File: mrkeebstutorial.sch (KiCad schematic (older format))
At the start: 153 parts, among them J1 USB_B_Mini, SW1 tilde/esc, SW10 9, SW11 0, SW12 _, SW13 =/+, SW14 Backspace_200, SW15 M1, SW16 Tab_150, SW17 Q, SW18 W, SW19 E, SW2 1, SW20 R, SW21 T, SW22 Y, SW23 U, SW24 I, SW25 O, SW26 P, SW27 {, SW28 }, SW29 \\, SW3 2, SW30 M2, SW31 Caps, SW32 A, SW33 S, SW34 D, SW35 F, SW36 G, SW37 H, SW38 J, SW39 K, SW4 3, SW40 L, SW41 :, SW42 \", SW43 Enter_2.25, SW44 M3, SW45 LShift_225, SW46 z, SW47 x, SW48 c, SW49 v, SW5 4, SW50 b, SW51 n, SW52 m, SW53 <, SW54 >, SW55 ?, SW56 R-shift_175, SW57 UP, SW58 M4, SW59 LCTRL, SW6 5, SW60 Win, SW61 Alt, SW62 Space, SW63 Alt, SW64 Win, SW65 Menu, SW66 LEFT, SW67 DOWN, SW68 RIGHT, SW7 6, SW8 7, SW9 8, U1 ATmega32U4-AU, Y1 16MHz

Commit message: finish routing draf
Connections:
- net Col15: no longer D31.1 (K), D32.1 (K), D33.1 (K), D34.1 (K), D35.1 (K), D36.1 (K), D37.1 (K), D38.1 (K), D39.1 (K), D40.1 (K), D41.1 (K), D42.1 (K), D43.1 (K), D44.1 (K), U1.27 (PD7)
- new net Row3: D31.1 (K), D32.1 (K), D33.1 (K), D34.1 (K), D35.1 (K), D36.1 (K), D37.1 (K), D38.1 (K), D39.1 (K), D40.1 (K), D41.1 (K), D42.1 (K), D43.1 (K), D44.1 (K), U1.27 (PD7)
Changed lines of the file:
@@
 Wire Wire Line
 	-3400 -300 -3300 -300
-Wire Wire Line
-	-3400 -275 -3400 -300
-$Comp
-L Switch:SW_Push SWP1
-U 1 1 5F0AD91B
-P -3400 -75
-F 0 "SWP1" H -3300 175 50  0000 R CNN
-F 1 "SW_Push" H -3200 100 50  0000 R CNN
-F 2 "random-keyboard-parts:SKQG-1155865" H -3400 125 50  0001 C CNN
-F 3 "~" H -3400 125 50  0001 C CNN
-	1    -3400 -75
-	0    -1   -1   0
-$EndComp
 Text GLabel -3000 -300 2    50   Output ~ 0
 RST
@@
 Wire Wire Line
 	15300 2950 15300 3950
-Wire Wire Line
-	15300 3950 15300 4325
 Connection ~ 15300 3950
 $Comp
@@
 $EndComp
 Wire Wire Line
-	15300 4325 15850 4325
-Wire Wire Line
 	15850 4325 15850 4400
-Connection ~ 15300 4325
 Connection ~ 14400 3950
 Wire Wire Line
@@
 Wire Wire Line
 	13475 3950 13475 5950
-Wire Wire Line
-	14925 4325 15300 4325
 Connection ~ 14925 4325
 Connection ~ 13075 4325
@@
 Wire Wire Line
 	13075 4325 14925 4325
-Wire Wire Line
-	15300 4325 15300 4950
 Wire Wire Line
 	15300 4950 15500 4950
@@
 Text GLabel -1000 2300 2    50   Input ~ 0
 Col9
+$Comp
+L Switch:SW_Push SWP1
+U 1 1 5F0AD91B
+P -3400 -75
+F 0 "SWP1" H -3300 175 50  0000 R CNN
+F 1 "SW_Push" H -3200 100 50  0000 R CNN
+F 2 "random-keyboard-parts:SKQG-1155865" H -3400 125 50  0001 C CNN
+F 3 "~" H -3400 125 50  0001 C CNN
+	1    -3400 -75
+	0    -1   -1   0
+$EndComp
+Wire Wire Line
+	-3400 -275 -3400 -300
+Wire Wire Line
+	15300 3950 15300 4950
+Wire Wire Line
+	14925 4325 15850 4325
 $EndSCHEMATC

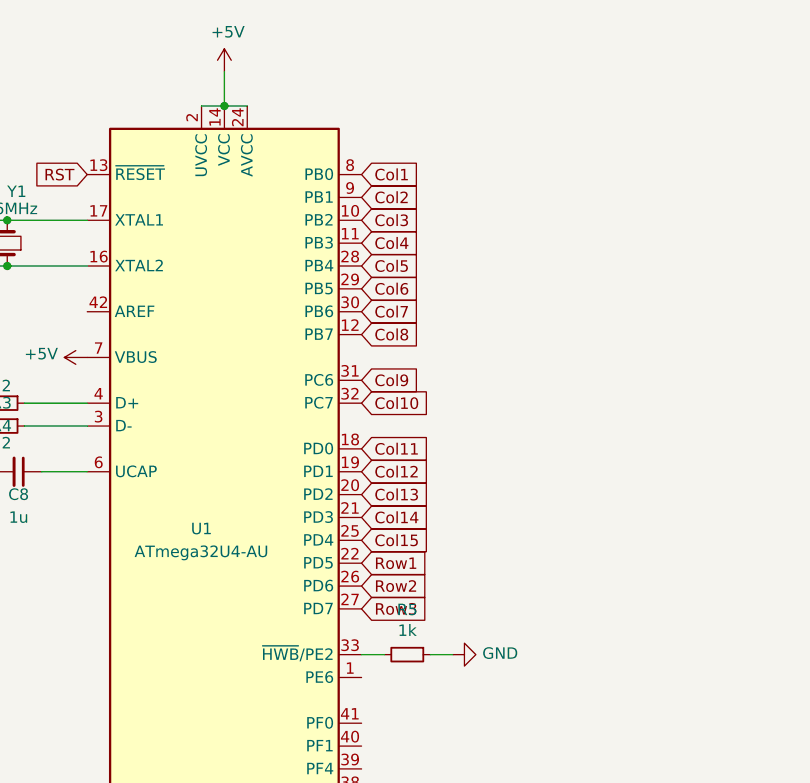
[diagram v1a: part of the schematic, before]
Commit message: routed some lines cleanly
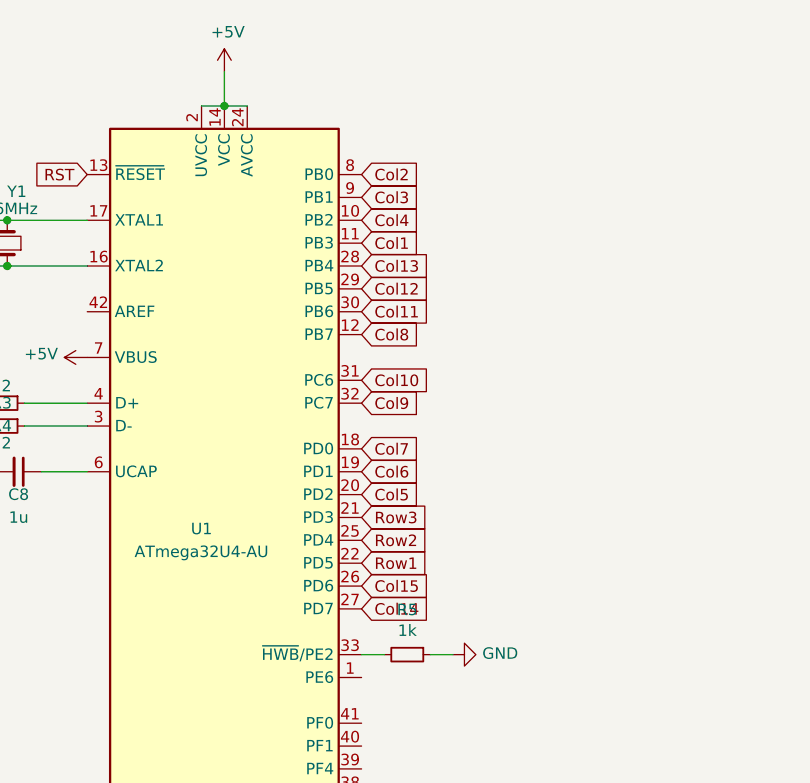
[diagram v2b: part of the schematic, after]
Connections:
- net Col1: now also U1.11 (PB3); no longer U1.8 (PB0)
- net Col10: now also U1.31 (PC6); no longer U1.32 (PC7)
- net Col11: now also U1.30 (PB6); no longer U1.18 (PD0)
- net Col12: now also U1.29 (PB5); no longer U1.19 (PD1)
- net Col13: now also U1.28 (PB4); no longer U1.20 (PD2)
- net Col14: now also U1.27 (PD7); no longer U1.21 (PD3)
- net Col15: now also U1.26 (PD6); no longer U1.25 (PD4)
- net Col2: now also U1.8 (PB0); no longer U1.9 (PB1)
- net Col3: now also U1.9 (PB1); no longer U1.10 (PB2)
- net Col4: now also U1.10 (PB2); no longer U1.11 (PB3)
- net Col5: now also U1.20 (PD2); no longer U1.28 (PB4)
- net Col6: now also U1.19 (PD1); no longer U1.29 (PB5)
- net Col7: now also U1.18 (PD0); no longer U1.30 (PB6)
- net Col9: now also U1.32 (PC7); no longer U1.31 (PC6)
- net Row2: now also U1.25 (PD4); no longer U1.26 (PD6)
- net Row3: now also U1.21 (PD3); no longer U1.27 (PD7)
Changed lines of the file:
@@
 	-1600 1100 -1600 950
 Connection ~ -1600 1100
-$Comp
-L MCU_Microchip_ATmega:ATmega32U4-AU U1
-U 1 1 5F06311B
-P -1600 2900
-F 0 "U1" H -1700 2850 50  0000 C CNN
-F 1 "ATmega32U4-AU" H -1700 2750 50  0000 C CNN
-F 2 "Package_QFP:TQFP-44_10x10mm_P0.8mm" H -1600 2900 50  0001 C CIN
-F 3 "http://ww1.microchip.com/downloads/en/DeviceDoc/Atmel-7766-8-bit-AVR-ATmega16U4-32U4_Datasheet.pdf" H -1600 2900 50  0001 C CNN
-	1    -1600 2900
-	1    0    0    -1
-$EndComp
 Connection ~ 2900 2300
 $Comp
@@
 Wire Wire Line
 	14000 6400 13075 6400
-Text GLabel -1000 3300 2    50   Input ~ 0
+Text GLabel -1000 2900 2    50   Input ~ 0
 Row3
-Text GLabel -1000 3200 2    50   Input ~ 0
+Text GLabel -1000 3000 2    50   Input ~ 0
 Row2
 Text GLabel -1000 3100 2    50   Input ~ 0
 Row1
-Text GLabel -1000 3000 2    50   Input ~ 0
+Text GLabel -1000 3200 2    50   Input ~ 0
 Col15
-Text GLabel -1000 2900 2    50   Input ~ 0
+Text GLabel -1000 3300 2    50   Input ~ 0
 Col14
-Text GLabel -1000 2800 2    50   Input ~ 0
+Text GLabel -1000 1800 2    50   Input ~ 0
 Col13
-Text GLabel -1000 2700 2    50   Input ~ 0
+Text GLabel -1000 1900 2    50   Input ~ 0
 Col12
-Text GLabel -1000 2600 2    50   Input ~ 0
-Col11
-Text GLabel -1000 2400 2    50   Input ~ 0
+Text GLabel -1000 2300 2    50   Input ~ 0
 Col10
 Text GLabel -1000 2100 2    50   Input ~ 0
 Col8
-Text GLabel -1000 2000 2    50   Input ~ 0
+Text GLabel -1000 2600 2    50   Input ~ 0
 Col7
-Text GLabel -1000 1900 2    50   Input ~ 0
+Text GLabel -1000 2700 2    50   Input ~ 0
 Col6
-Text GLabel -1000 1800 2    50   Input ~ 0
+Text GLabel -1000 2800 2    50   Input ~ 0
 Col5
-Text GLabel -1000 1700 2    50   Input ~ 0
-Col4
-Text GLabel -1000 1600 2    50   Input ~ 0
-Col3
-Text GLabel -1000 1500 2    50   Input ~ 0
-Col2
-Text GLabel -1000 1400 2    50   Input ~ 0
-Col1
-Text GLabel -1000 2300 2    50   Input ~ 0
+Text GLabel -1000 2400 2    50   Input ~ 0
 Col9
 $Comp
@@
 Wire Wire Line
 	14925 4325 15850 4325
+Text GLabel -1000 1700 2    50   Input ~ 0
+Col1
+Text GLabel -1000 1400 2    50   Input ~ 0
+Col2
+Text GLabel -1000 1500 2    50   Input ~ 0
+Col3
+Text GLabel -1000 1600 2    50   Input ~ 0
+Col4
+$Comp
+L MCU_Microchip_ATmega:ATmega32U4-AU U1
+U 1 1 5F06311B
+P -1600 2900
+F 0 "U1" H -1700 2850 50  0000 C CNN
+F 1 "ATmega32U4-AU" H -1700 2750 50  0000 C CNN
+F 2 "Package_QFP:TQFP-44_10x10mm_P0.8mm" H -1600 2900 50  0001 C CIN
+F 3 "http://ww1.microchip.com/downloads/en/DeviceDoc/Atmel-7766-8-bit-AVR-ATmega16U4-32U4_Datasheet.pdf" H -1600 2900 50  0001 C CNN
+	1    -1600 2900
+	1    0    0    -1
+$EndComp
+Text GLabel -1000 2000 2    50   Input ~ 0
+Col11
 $EndSCHEMATC

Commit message: rearranged
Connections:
- net Col1: now also U1.12 (PB7); no longer U1.11 (PB3)
- net Col8: now also U1.25 (PD4); no longer U1.12 (PB7)
- net Row2: now also U1.40 (PF1); no longer U1.25 (PD4)
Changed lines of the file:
@@
 Text GLabel -1000 2900 2    50   Input ~ 0
 Row3
-Text GLabel -1000 3000 2    50   Input ~ 0
+Text GLabel -1000 3900 2    50   Input ~ 0
 Row2
 Text GLabel -1000 3100 2    50   Input ~ 0
@@
 Text GLabel -1000 2300 2    50   Input ~ 0
 Col10
-Text GLabel -1000 2100 2    50   Input ~ 0
-Col8
 Text GLabel -1000 2600 2    50   Input ~ 0
 Col7
@@
 Wire Wire Line
 	14925 4325 15850 4325
-Text GLabel -1000 1700 2    50   Input ~ 0
+Text GLabel -1000 2100 2    50   Input ~ 0
 Col1
 Text GLabel -1000 1400 2    50   Input ~ 0
@@
 	1    0    0    -1
 $EndComp
+Text GLabel -1000 3000 2    50   Input ~ 0
+Col8
 Text GLabel -1000 2000 2    50   Input ~ 0
 Col11

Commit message: routed second thing
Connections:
- net Col1: now also U1.21 (PD3); no longer U1.12 (PB7)
- net Col5: now also U1.1 (PE6); no longer U1.20 (PD2)
- net Col6: now also U1.41 (PF0); no longer U1.19 (PD1)
- net Col7: now also U1.40 (PF1); no longer U1.18 (PD0)
- net Row2: now also U1.36 (PF7); no longer U1.40 (PF1)
- net Row3: now also U1.19 (PD1); no longer U1.21 (PD3)
- net Row4: now also U1.18 (PD0)
- net Row5: now also U1.12 (PB7)
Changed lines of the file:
@@
 Wire Wire Line
 	13475 6950 13650 6950
-Text GLabel 1750 6400 0    50   Input ~ 0
-Row5
 Connection ~ 13475 5950
 $Comp
@@
 Wire Wire Line
 	14000 6400 13075 6400
-Text GLabel -1000 2900 2    50   Input ~ 0
+Text GLabel -1000 2700 2    50   Input ~ 0
 Row3
-Text GLabel -1000 3900 2    50   Input ~ 0
+Text GLabel -1000 4300 2    50   Input ~ 0
 Row2
 Text GLabel -1000 3100 2    50   Input ~ 0
@@
 Text GLabel -1000 2300 2    50   Input ~ 0
 Col10
-Text GLabel -1000 2600 2    50   Input ~ 0
+Text GLabel -1000 3900 2    50   Input ~ 0
 Col7
-Text GLabel -1000 2700 2    50   Input ~ 0
-Col6
-Text GLabel -1000 2800 2    50   Input ~ 0
-Col5
 Text GLabel -1000 2400 2    50   Input ~ 0
 Col9
@@
 Wire Wire Line
 	14925 4325 15850 4325
-Text GLabel -1000 2100 2    50   Input ~ 0
+Text GLabel -1000 2900 2    50   Input ~ 0
 Col1
 Text GLabel -1000 1400 2    50   Input ~ 0
 Col2
-Text GLabel -1000 1500 2    50   Input ~ 0
-Col3
-Text GLabel -1000 1600 2    50   Input ~ 0
-Col4
+Text GLabel -1000 3000 2    50   Input ~ 0
+Col8
+Text GLabel -1000 2000 2    50   Input ~ 0
+Col11
+Text GLabel -1000 3800 2    50   Input ~ 0
+Col6
 $Comp
 L MCU_Microchip_ATmega:ATmega32U4-AU U1
@@
 	1    0    0    -1
 $EndComp
-Text GLabel -1000 3000 2    50   Input ~ 0
-Col8
-Text GLabel -1000 2000 2    50   Input ~ 0
-Col11
+Text GLabel -1000 1600 2    50   Input ~ 0
+Col4
+Text GLabel -1000 1500 2    50   Input ~ 0
+Col3
+Text GLabel 1750 6400 0    50   Input ~ 0
+Row5
+Text GLabel -1000 2100 2    50   Input ~ 0
+Row5
+Text GLabel -1000 2600 2    50   Input ~ 0
+Row4
+Text GLabel -1000 3600 2    50   Input ~ 0
+Col5
 $EndSCHEMATC

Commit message: i think done
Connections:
- net Col2: now also U1.9 (PB1); no longer U1.8 (PB0)
- net Col3: now also U1.10 (PB2); no longer U1.9 (PB1)
- net Col4: now also U1.11 (PB3); no longer U1.10 (PB2)
- net RST: now also U1.37 (PF6); no longer U1.13 (~RESET)
- net Row2: now also U1.8 (PB0); no longer U1.36 (PF7)
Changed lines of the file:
@@
 	-1   0    0    1
 $EndComp
-Text GLabel -2200 1400 0    50   Input ~ 0
+Text GLabel -1000 4200 2    50   Input ~ 0
 RST
 Wire Wire Line
@@
 Text GLabel -1000 2700 2    50   Input ~ 0
 Row3
-Text GLabel -1000 4300 2    50   Input ~ 0
+Text GLabel -1000 1400 2    50   Input ~ 0
 Row2
 Text GLabel -1000 3100 2    50   Input ~ 0
@@
 Text GLabel -1000 2900 2    50   Input ~ 0
 Col1
-Text GLabel -1000 1400 2    50   Input ~ 0
+Text GLabel -1000 1500 2    50   Input ~ 0
 Col2
 Text GLabel -1000 3000 2    50   Input ~ 0
@@
 	1    0    0    -1
 $EndComp
+Text GLabel -1000 1700 2    50   Input ~ 0
+Col4
 Text GLabel -1000 1600 2    50   Input ~ 0
-Col4
-Text GLabel -1000 1500 2    50   Input ~ 0
 Col3
 Text GLabel 1750 6400 0    50   Input ~ 0

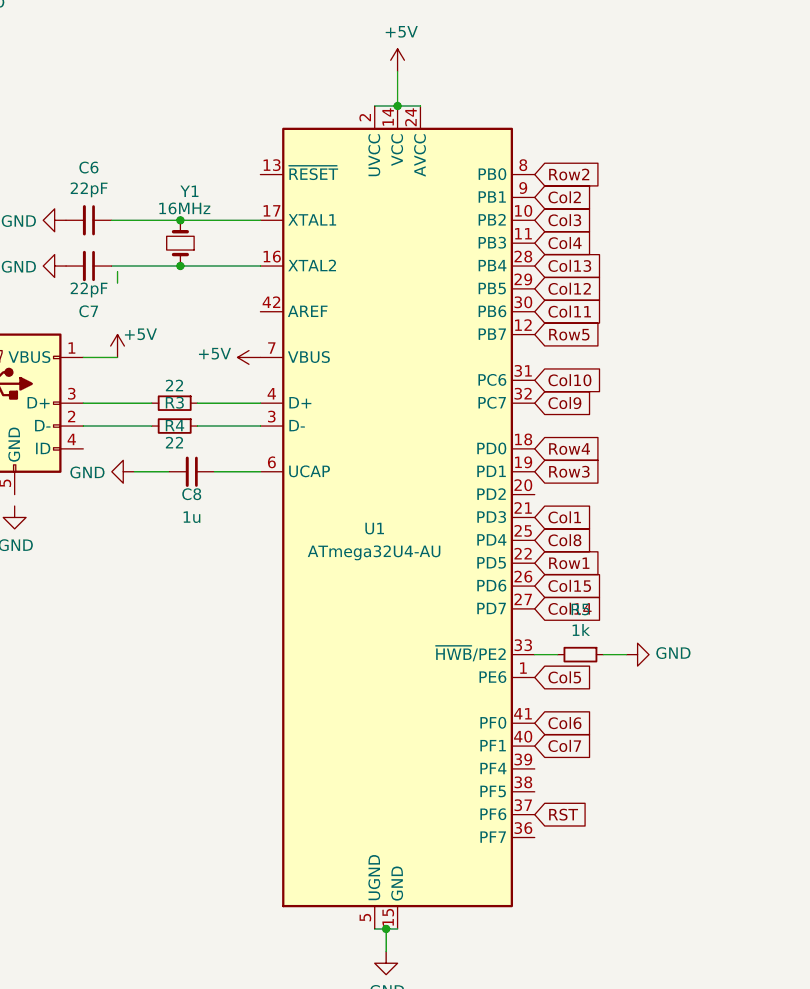
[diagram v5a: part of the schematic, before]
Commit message: changed ground plane
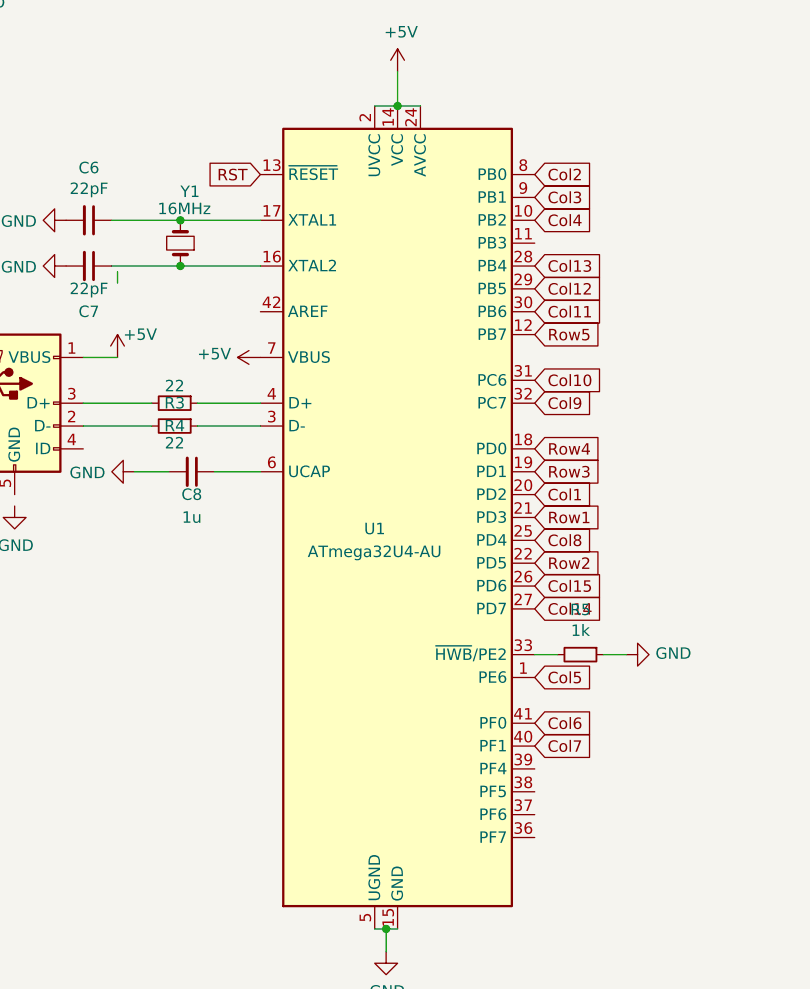
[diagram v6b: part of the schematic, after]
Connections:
- net Col1: now also U1.20 (PD2); no longer U1.21 (PD3)
- net Col2: now also U1.8 (PB0); no longer U1.9 (PB1)
- net Col3: now also U1.9 (PB1); no longer U1.10 (PB2)
- net Col4: now also U1.10 (PB2); no longer U1.11 (PB3)
- net RST: now also U1.13 (~RESET); no longer U1.37 (PF6)
- net Row1: now also U1.21 (PD3); no longer U1.22 (PD5)
- net Row2: now also U1.22 (PD5); no longer U1.8 (PB0)
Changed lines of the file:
@@
 	-1   0    0    1
 $EndComp
-Text GLabel -1000 4200 2    50   Input ~ 0
-RST
 Wire Wire Line
 	-700 3500 -600 3500
@@
 Wire Wire Line
 	14000 6400 13075 6400
-Text GLabel -1000 2700 2    50   Input ~ 0
-Row3
-Text GLabel -1000 1400 2    50   Input ~ 0
-Row2
-Text GLabel -1000 3100 2    50   Input ~ 0
+Text GLabel -1000 2900 2    50   Input ~ 0
 Row1
 Text GLabel -1000 3200 2    50   Input ~ 0
@@
 Wire Wire Line
 	14925 4325 15850 4325
-Text GLabel -1000 2900 2    50   Input ~ 0
-Col1
-Text GLabel -1000 1500 2    50   Input ~ 0
+Text GLabel -1000 1400 2    50   Input ~ 0
 Col2
 Text GLabel -1000 3000 2    50   Input ~ 0
@@
 Text GLabel -1000 3800 2    50   Input ~ 0
 Col6
-$Comp
-L MCU_Microchip_ATmega:ATmega32U4-AU U1
-U 1 1 5F06311B
-P -1600 2900
-F 0 "U1" H -1700 2850 50  0000 C CNN
-F 1 "ATmega32U4-AU" H -1700 2750 50  0000 C CNN
-F 2 "Package_QFP:TQFP-44_10x10mm_P0.8mm" H -1600 2900 50  0001 C CIN
-F 3 "http://ww1.microchip.com/downloads/en/DeviceDoc/Atmel-7766-8-bit-AVR-ATmega16U4-32U4_Datasheet.pdf" H -1600 2900 50  0001 C CNN
-	1    -1600 2900
-	1    0    0    -1
-$EndComp
-Text GLabel -1000 1700 2    50   Input ~ 0
+Text GLabel -1000 1600 2    50   Input ~ 0
 Col4
-Text GLabel -1000 1600 2    50   Input ~ 0
+Text GLabel -1000 1500 2    50   Input ~ 0
 Col3
 Text GLabel 1750 6400 0    50   Input ~ 0
@@
 Text GLabel -1000 3600 2    50   Input ~ 0
 Col5
+Text GLabel -1000 3100 2    50   Input ~ 0
+Row2
+Text GLabel -1000 2800 2    50   Input ~ 0
+Col1
+Text GLabel -1000 2700 2    50   Input ~ 0
+Row3
+$Comp
+L MCU_Microchip_ATmega:ATmega32U4-AU U1
+U 1 1 5F06311B
+P -1600 2900
+F 0 "U1" H -1700 2850 50  0000 C CNN
+F 1 "ATmega32U4-AU" H -1700 2750 50  0000 C CNN
+F 2 "Package_QFP:TQFP-44_10x10mm_P0.8mm" H -1600 2900 50  0001 C CIN
+F 3 "http://ww1.microchip.com/downloads/en/DeviceDoc/Atmel-7766-8-bit-AVR-ATmega16U4-32U4_Datasheet.pdf" H -1600 2900 50  0001 C CNN
+	1    -1600 2900
+	1    0    0    -1
+$EndComp
+Text GLabel -2200 1400 0    50   Input ~ 0
+RST
 $EndSCHEMATC

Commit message: migraterd dshit
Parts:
- R3, R4: LCSC (none) -> 22

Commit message: changed components for BOM
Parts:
- C1: LCSC (none) -> C1713
- C2, C8: LCSC (none) -> C28323
- C3, C4, C5: LCSC (none) -> C129690
- C6, C7: LCSC (none) -> C465168
- D1, D10, D11, D12, D13, D14, D15, D16, D17, D18, D19, D2, D20, D21, D22, D23, D24, D25, D26, D27, D28, D29, D3, D30, D31, D32, D33, D34, D35, D36, D37, D38, D39, D4, D40, D41, D42, D43, D44, D45, D46, D47, D48, D49, D5, D50, D51, D52, D53, D54, D55, D56, D57, D58, D59, D6, D60, D61, D62, D63, D64, D65, D66, D67, D68, D7, D8, D9: LCSC (none) -> C402213
- R1: footprint Resistor_SMD:R_1206_3216Metric_Pad1.42x1.75mm_HandSolder -> Resistor_SMD:R_0805_2012Metric_Pad1.15x1.40mm_HandSolder; LCSC (none) -> C104602
- R2: footprint Resistor_SMD:R_1206_3216Metric_Pad1.42x1.75mm_HandSolder -> Resistor_SMD:R_0805_2012Metric_Pad1.15x1.40mm_HandSolder; LCSC (none) -> C104769
- R3, R4: footprint Resistor_SMD:R_1206_3216Metric_Pad1.42x1.75mm_HandSolder -> Resistor_SMD:R_0805_2012Metric_Pad1.15x1.40mm_HandSolder; LCSC 22 -> C399501
- R5: footprint Resistor_SMD:R_1206_3216Metric_Pad1.42x1.75mm_HandSolder -> Resistor_SMD:R_0805_2012Metric_Pad1.15x1.40mm_HandSolder; LCSC (none) -> C510146
- SWP1: footprint random-keyboard-parts:SKQG-1155865 -> random-keyboard-parts:PushButton_6x6mm_TH
- U1: LCSC (none) -> C44854
- Y1: LCSC (none) -> C115962
